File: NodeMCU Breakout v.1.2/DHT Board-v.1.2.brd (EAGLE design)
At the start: 42.8 x 54.6 mm, 13 parts, among them IC1 74HCT125N

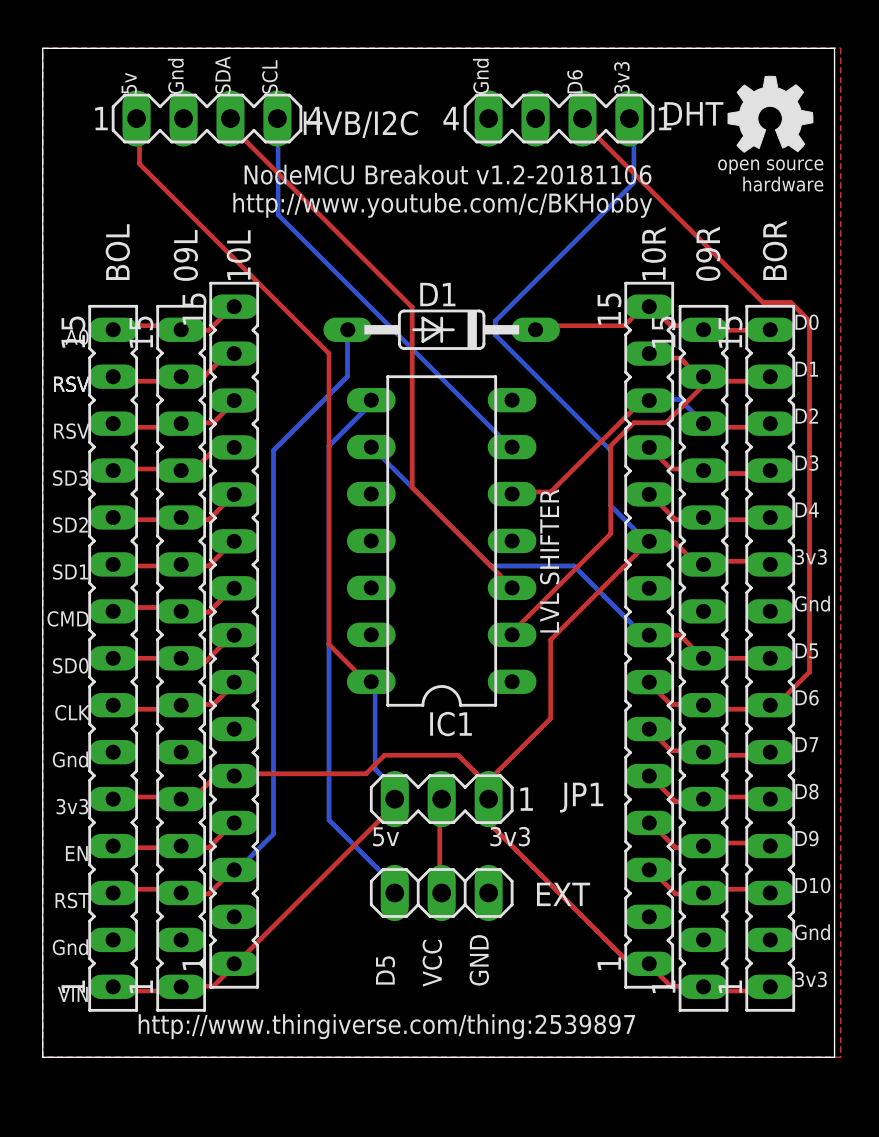
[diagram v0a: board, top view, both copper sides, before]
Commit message: 12/26/18(BK): Updated with changes to EXT signal (D4, to make it compatible with all LED drivers), adding another pin to the I2C/HVB header, and adding a set of solder jumpers on the back of the board, for bypassing the level shifter as necessary.
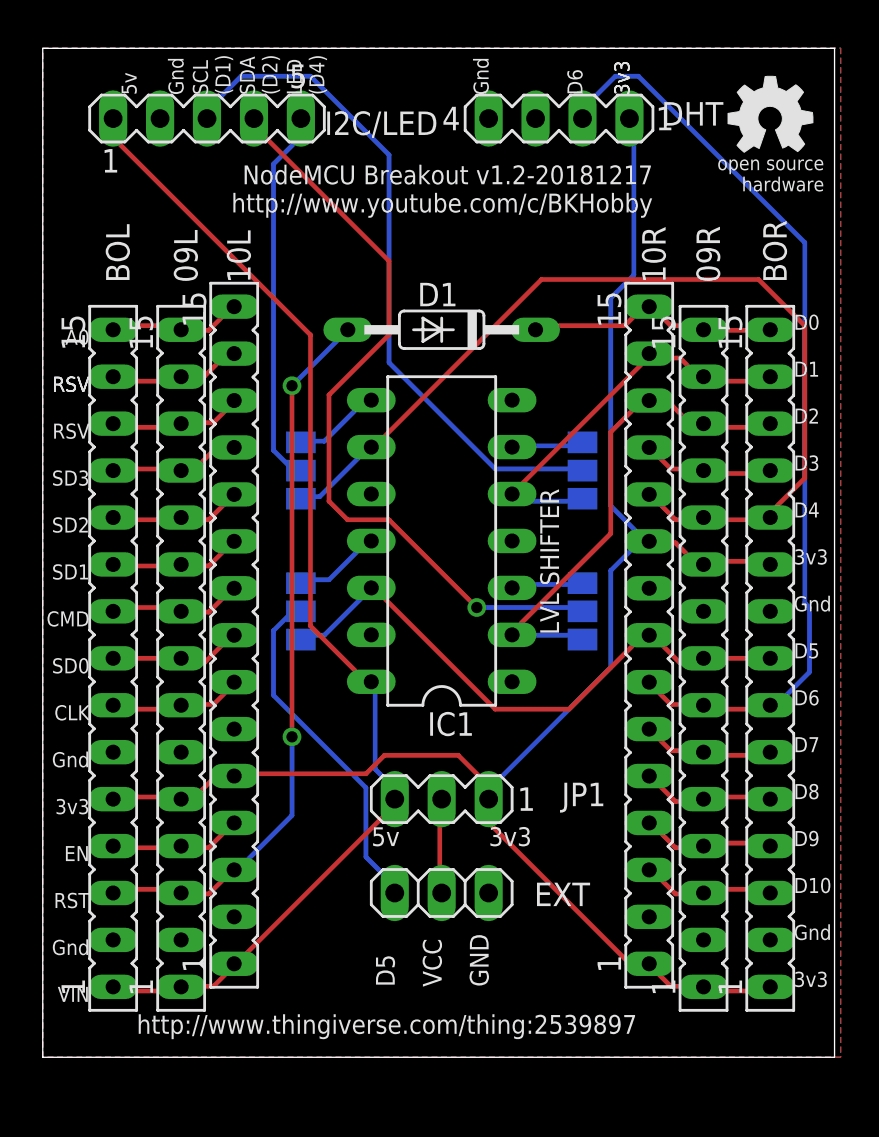
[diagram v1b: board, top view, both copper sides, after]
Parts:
- removed HVB/I2C: (no value), con-lstb:MA04-1
- added D1BYP, D2BYP, D4BYP, D5BYP: (no value), jumper:SJ_2
- added I2C/LED: (no value), con-lstb:MA05-1
- added U$2: (no value), oshw:OSHW_5MM
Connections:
- removed net SCL/D2: HVB/I2C.4, IC1.6
- removed net SDA/D1: HVB/I2C.3, IC1.3
- new net EXTD5: D5BYP.2, EXT.1
- new net HD1: D1BYP.3, IC1.6
- new net HD2: D2BYP.3, IC1.3
- new net HD4: D4BYP.3, IC1.8
- new net LED/D4: D4BYP.2, I2C/LED.5
- new net SCL/D1: D1BYP.2, I2C/LED.3
- new net SDA/D2: D2BYP.2, I2C/LED.4
- net 5V: now also I2C/LED.1; no longer HVB/I2C.1
- net D1: now also D1BYP.1, IC1.5; no longer IC1.2
- net D2: now also D2BYP.1, IC1.2; no longer IC1.5
- net D4: now also D4BYP.1, IC1.9
- net D5: now also D5BYP.1, IC1.12; no longer IC1.9
- net GND: now also I2C/LED.2, IC1.13; no longer HVB/I2C.2
- net HD5: now also D5BYP.3, IC1.11; no longer EXT.1, IC1.8
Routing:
- net D4: track 7.28 -> 51.9 mm
- net SDA/D2: track 0.00 -> 41.4 mm, vias 0 -> 1
- net SCL/D1: track 0.00 -> 37.0 mm
- net SDA/D1: track 31.8 -> 0.00 mm
- net HD5: track 29.2 -> 5.02 mm
- net SCL/D2: track 23.1 -> 0.00 mm
- net LED/D4: track 0.00 -> 20.5 mm
- net EXTD5: track 0.00 -> 19.0 mm
- net D2: track 16.9 -> 27.2 mm
- net D5: track 26.3 -> 31.8 mm
- net HD4: track 0.00 -> 4.87 mm
- net 3.3V: track 97.8 -> 93.0 mm
- net D1: track 26.8 -> 22.3 mm
- net D6: track 46.3 -> 50.7 mm
- net HD2: track 0.00 -> 3.94 mm
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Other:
- board text added: "BYP"
- board text added: "LED (D4)"
- board text added: "NodeMCU Breakout v1.2-20181217 http://www.youtube.com/c/BKHobby"
- board text added: "SCL (D1)"
- board text added: "SDA (D2)"
- board text added: "SHFT"
- board text removed: "NodeMCU Breakout v1.2-20181106 http://www.youtube.com/c/BKHobby"
- board text removed: "SCL"
- board text removed: "SDA"

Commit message: Updated to add I2C_VCC selector solder bridge (3.3/5v supply) and mounting holes.
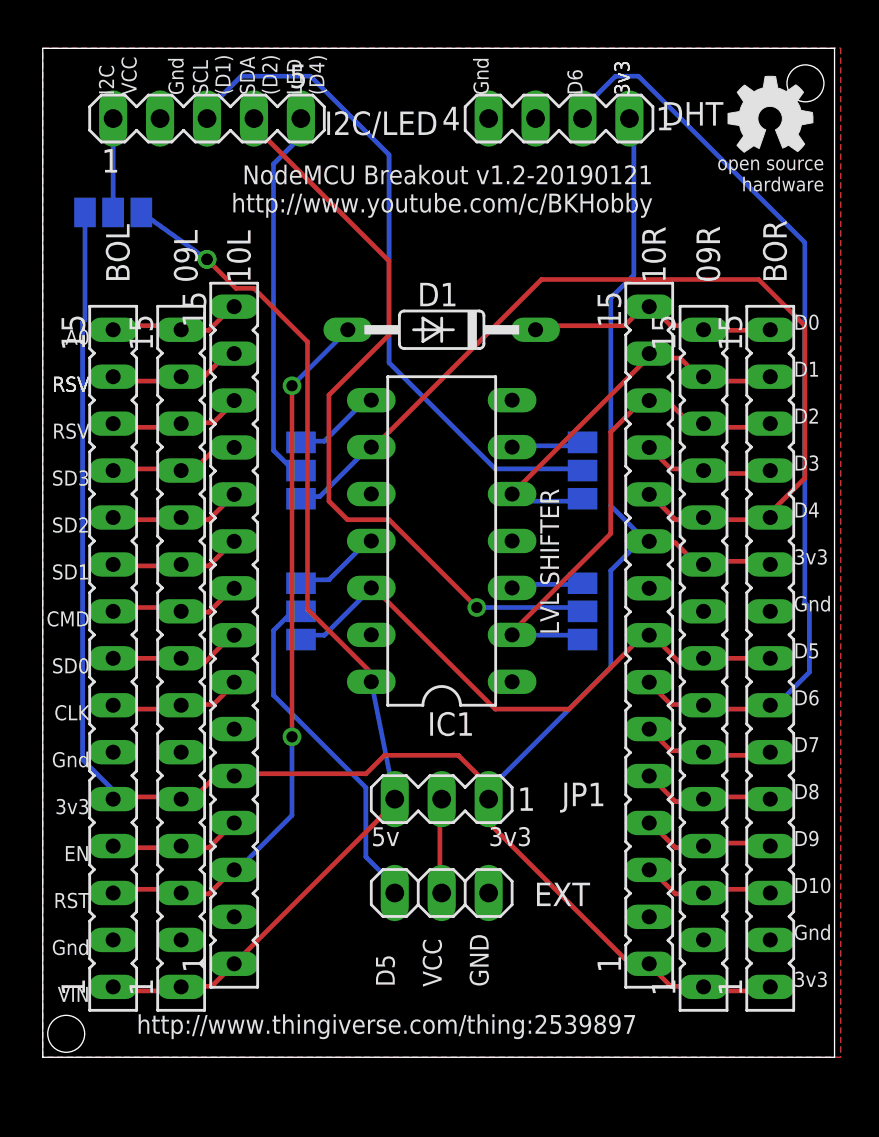
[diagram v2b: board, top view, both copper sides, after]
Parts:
- added I2C_VCC: (no value), jumper:SJ_2
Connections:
- new net I2C_VCC: I2C/LED.1, I2C_VCC.2
- net 3.3V: now also I2C_VCC.1
- net 5V: now also I2C_VCC.3; no longer I2C/LED.1
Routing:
- net 3.3V: track 93.0 -> 125.5 mm
- net 5V: track 63.8 -> 58.7 mm, vias 0 -> 1
- net I2C_VCC: track 0.00 -> 5.08 mm
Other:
- board text added: "3.3V"
- board text added: "5V"
- board text added: "I2C VCC"
- board text added: "NodeMCU Breakout v1.2-20190121 http://www.youtube.com/c/BKHobby"
- board text removed: "NodeMCU Breakout v1.2-20181217 http://www.youtube.com/c/BKHobby"
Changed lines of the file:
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@@
 <layer number="43" name="vRestrict" color="2" fill="10" visible="yes" active="yes"/>
 <layer number="44" name="Drills" color="7" fill="1" visible="no" active="yes"/>
-<layer number="45" name="Holes" color="7" fill="1" visible="no" active="yes"/>
+<layer number="45" name="Holes" color="7" fill="1" visible="yes" active="yes"/>
 <layer number="46" name="Milling" color="3" fill="1" visible="no" active="yes"/>
 <layer number="47" name="Measures" color="7" fill="1" visible="yes" active="yes"/>
@@
 <wire x1="59.36" y1="64.76" x2="16.51" y2="64.76" width="0" layer="20"/>
 <wire x1="16.51" y1="64.76" x2="16.51" y2="10.16" width="0" layer="20"/>
-<text x="49.53" y="58.42" size="1.016" layer="25" rot="R180">NodeMCU Breakout v1.2-20181217
+<text x="49.53" y="58.42" size="1.016" layer="25" rot="R180">NodeMCU Breakout v1.2-20190121
 http://www.youtube.com/c/BKHobby</text>
 <text x="38.1" y="13.97" size="1.016" layer="25" rot="R90">VCC</text>
@@
 <text x="34.29" y="21.59" size="1.016" layer="25">5v</text>
 <text x="40.64" y="21.59" size="1.016" layer="25">3v3</text>
-<text x="21.59" y="62.23" size="0.8128" layer="25" rot="R90">5v</text>
+<text x="21.59" y="62.23" size="0.8128" layer="25" rot="R90">I2C
+VCC</text>
 <text x="40.64" y="62.23" size="0.8128" layer="25" rot="R90">Gnd</text>
 <text x="24.13" y="62.23" size="0.8128" layer="25" rot="R90">Gnd</text>
@@
 <text x="29.21" y="38.1" size="0.8128" layer="26" rot="MR180">SHFT</text>
 <text x="44.45" y="38.1" size="0.8128" layer="26" rot="MR180">SHFT</text>
-<text x="22.86" y="58.42" size="1.016" layer="26" rot="MR180">NodeMCU Breakout v1.2-20181217
+<text x="22.86" y="58.42" size="1.016" layer="26" rot="MR180">NodeMCU Breakout v1.2-20190121
 http://www.youtube.com/c/BKHobby</text>
 <text x="53.34" y="11.43" size="1.016" layer="26" rot="MR0">http://www.thingiverse.com/thing:2539897</text>
+<text x="21.59" y="54.61" size="0.8128" layer="26" rot="MR180">5V</text>
+<text x="19.05" y="54.61" size="0.8128" layer="26" rot="MR180">3.3V</text>
+<text x="17.78" y="54.61" size="0.8128" layer="26" rot="MR180">3.3V</text>
+<hole x="57.785" y="62.865" drill="2"/>
+<hole x="17.78" y="11.43" drill="2"/>
 </plain>
 <attributes>
@@
 <autorouter>
 <pass name="Default">
-<param name="RoutingGrid" value="0.125mm"/>
+<param name="RoutingGrid" value="0.25mm"/>
 <param name="AutoGrid" value="1"/>
 <param name="Efforts" value="2"/>
@@
 </element>
 <element name="U$2" library="oshw" package="OSHW_5MM" value="" x="55.88" y="60.96" smashed="yes" rot="MR0"/>
+<element name="I2C_VCC" library="jumper" library_urn="urn:adsk.eagle:library:252" package="SJ_2" package3d_urn="urn:adsk.eagle:package:15474/1" value="" x="20.32" y="55.88" smashed="yes" rot="MR180">
+<attribute name="NAME" x="24.257" y="57.15" size="1.27" layer="26" ratio="10" rot="MR358.9"/>
+<attribute name="VALUE" x="20.2199" y="55.88" size="0.02" layer="28" rot="MR180"/>
+</element>
 </elements>
 <signals>
@@
 <wire x1="24" y1="21.5" x2="24" y2="21.59" width="0.254" layer="1"/>
 </signal>
+<signal name="I2C_VCC">
+<contactref element="I2C/LED" pad="1"/>
+<contactref element="I2C_VCC" pad="2"/>
+<wire x1="20.32" y1="55.88" x2="20.32" y2="60.96" width="0.254" layer="16"/>
+</signal>
 <signal name="5V">
 <contactref element="10L" pad="1"/>
 <contactref element="09L" pad="1"/>
 <contactref element="JP1" pad="3"/>
-<contactref element="I2C/LED" pad="1"/>
 <contactref element="IC1" pad="14"/>
 <contactref element="BOL" pad="1"/>
@@
 <wire x1="20.5" y1="13.75" x2="20.32" y2="13.97" width="0.254" layer="1"/>
 <wire x1="24" y1="13.75" x2="24" y2="13.97" width="0.254" layer="1"/>
-<wire x1="25.75" y1="14" x2="26.75" y2="15" width="0.254" layer="1"/>
-<wire x1="24" y1="14" x2="25.75" y2="14" width="0.254" layer="1"/>
-<wire x1="26.75" y1="15" x2="26.87" y2="15.22" width="0.254" layer="1"/>
+<wire x1="24" y1="14" x2="25.65" y2="14" width="0.254" layer="1"/>
+<wire x1="25.65" y1="14" x2="25.75" y2="14" width="0.254" layer="1"/>
 <wire x1="24" y1="14" x2="24" y2="13.97" width="0.254" layer="1"/>
-<wire x1="34.5" y1="25.75" x2="34.5" y2="30.25" width="0.254" layer="16"/>
-<wire x1="35.5" y1="24.75" x2="34.5" y2="25.75" width="0.254" layer="16"/>
-<wire x1="35.5" y1="24.25" x2="35.5" y2="24.75" width="0.254" layer="16"/>
 <wire x1="34.5" y1="30.25" x2="34.29" y2="30.48" width="0.254" layer="16"/>
 <wire x1="35.5" y1="24.25" x2="35.56" y2="24.13" width="0.254" layer="16"/>
-<wire x1="20.5" y1="59.75" x2="20.5" y2="60.75" width="0.254" layer="1"/>
-<wire x1="31" y1="49.25" x2="20.5" y2="59.75" width="0.254" layer="1"/>
-<wire x1="31" y1="33.5" x2="31" y2="49.25" width="0.254" layer="1"/>
-<wire x1="34.25" y1="30.25" x2="31" y2="33.5" width="0.254" layer="1"/>
-<wire x1="20.5" y1="60.75" x2="20.32" y2="60.96" width="0.254" layer="1"/>
 <wire x1="34.25" y1="30.25" x2="34.29" y2="30.48" width="0.254" layer="1"/>
-<wire x1="35.75" y1="24" x2="27" y2="15.25" width="0.254" layer="1"/>
-<wire x1="27" y1="15.25" x2="26.87" y2="15.22" width="0.254" layer="1"/>
-<wire x1="35.75" y1="24" x2="35.56" y2="24.13" width="0.254" layer="1"/>
+<contactref element="I2C_VCC" pad="3"/>
+<wire x1="25.65" y1="14" x2="26.87" y2="15.22" width="0.254" layer="1"/>
+<wire x1="26.87" y1="15.22" x2="35.56" y2="23.91" width="0.254" layer="1"/>
+<wire x1="35.56" y1="23.91" x2="35.56" y2="24.13" width="0.254" layer="1"/>
+<wire x1="35.56" y1="24.13" x2="34.29" y2="30.48" width="0.254" layer="16"/>
+<wire x1="34.29" y1="30.48" x2="34.29" y2="30.958675" width="0.254" layer="1"/>
+<wire x1="27.940725" y1="51.7706" x2="26.9694" y2="51.7706" width="0.254" layer="1"/>
+<wire x1="34.29" y1="30.958675" x2="30.8382" y2="34.410475" width="0.254" layer="1"/>
+<wire x1="30.8382" y1="34.410475" x2="30.8382" y2="48.873125" width="0.254" layer="1"/>
+<wire x1="30.8382" y1="48.873125" x2="27.940725" y2="51.7706" width="0.254" layer="1"/>
+<wire x1="26.9694" y1="51.7706" x2="25.4" y2="53.34" width="0.254" layer="1"/>
+<via x="25.4" y="53.34" extent="1-16" drill="0.6096"/>
+<wire x1="25.4" y1="53.34" x2="21.844" y2="55.88" width="0.254" layer="16"/>
 </signal>
 <signal name="N$1">
@@
 <wire x1="49" y1="38.25" x2="49.33" y2="38.08" width="0.254" layer="16"/>
 <wire x1="40.75" y1="24.25" x2="40.64" y2="24.13" width="0.254" layer="16"/>
+<contactref element="I2C_VCC" pad="1"/>
+<wire x1="20.32" y1="24.13" x2="20.32" y2="24.608675" width="0.254" layer="16"/>
+<wire x1="18.669" y1="49.940325" x2="18.796" y2="50.067325" width="0.254" layer="16"/>
+<wire x1="18.796" y1="50.067325" x2="18.796" y2="55.88" width="0.254" layer="16"/>
+<wire x1="20.32" y1="24.608675" x2="18.669" y2="26.259675" width="0.254" layer="16"/>
+<wire x1="18.669" y1="26.259675" x2="18.669" y2="49.940325" width="0.254" layer="16"/>
 </signal>
 <signal name="D1">
@@
 <contactref element="IC1" pad="4"/>
 <contactref element="IC1" pad="1"/>
-<wire x1="41.91" y1="45.72" x2="40.64" y2="60.96" width="0" layer="19" extent="1-1"/>
-<wire x1="41.91" y1="38.1" x2="41.91" y2="45.72" width="0" layer="19" extent="1-1"/>
-<wire x1="41.91" y1="30.48" x2="41.91" y2="38.1" width="0" layer="19" extent="1-1"/>
-<wire x1="49.33" y1="35.54" x2="41.91" y2="38.1" width="0" layer="19" extent="1-1"/>
-<wire x1="52.27" y1="34.29" x2="49.33" y2="35.54" width="0" layer="19" extent="1-1"/>
-<wire x1="55.88" y1="34.29" x2="52.27" y2="34.29" width="0" layer="19" extent="1-1"/>
-<wire x1="34.29" y1="40.64" x2="41.91" y2="38.1" width="0" layer="19" extent="1-1"/>
-<wire x1="34.29" y1="33.02" x2="34.29" y2="40.64" width="0" layer="19" extent="1-1"/>
-<wire x1="26.87" y1="27.92" x2="34.29" y2="33.02" width="0" layer="19" extent="1-1"/>
-<wire x1="24" y1="26.67" x2="26.87" y2="27.92" width="0" layer="19" extent="1-1"/>
-<wire x1="20.32" y1="26.67" x2="24" y2="26.67" width="0" layer="19" extent="1-1"/>
-<wire x1="26.87" y1="17.76" x2="24" y2="26.67" width="0" layer="19" extent="1-1"/>
-<wire x1="24" y1="16.51" x2="26.87" y2="17.76" width="0" layer="19" extent="1-1"/>
-<wire x1="20.32" y1="16.51" x2="24" y2="16.51" width="0" layer="19" extent="1-1"/>
-<wire x1="40.64" y1="19.05" x2="41.91" y2="30.48" width="0" layer="19" extent="1-1"/>
-<wire x1="49.33" y1="17.76" x2="40.64" y2="19.05" width="0" layer="19" extent="1-1"/>
-<wire x1="52.27" y1="16.51" x2="49.33" y2="17.76" width="0" layer="19" extent="1-1"/>
-<wire x1="55.88" y1="16.51" x2="52.27" y2="16.51" width="0" layer="19" extent="1-1"/>
-<wire x1="22.86" y1="60.96" x2="40.64" y2="60.96" width="0" layer="19" extent="1-1"/>
 </signal>
 <signal name="CLK">
@@
 <wire x1="34.25" y1="38.25" x2="34.29" y2="38.1" width="0.254" layer="16"/>
 </signal>
+<signal name="N$2">
+<via x="25.4" y="53.34" extent="1-16" drill="0.6096"/>
+</signal>
 </signals>

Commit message: 2/2/19(BK): Updated rev 1.2 to final:
-Removed I2C_VCC Solder jumper and added 6th pin to the header (both 3.3v & 5v are brought out)
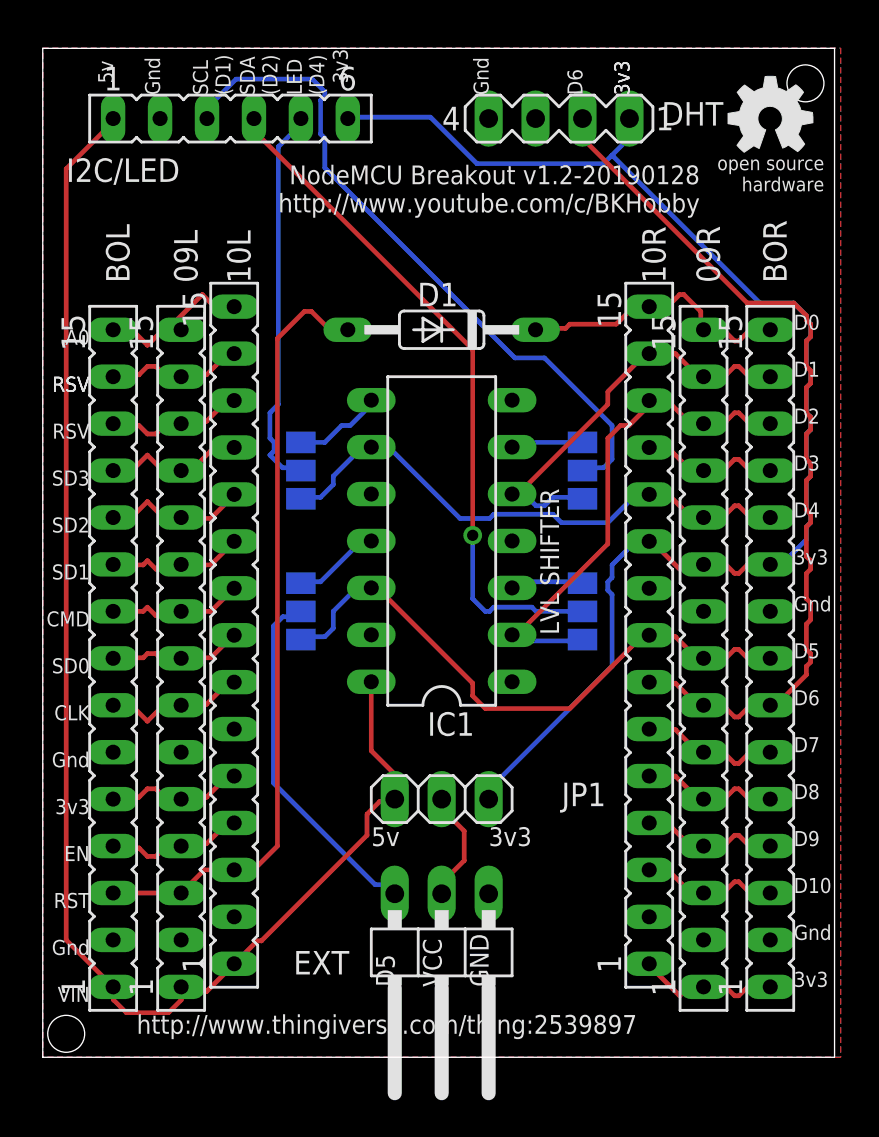
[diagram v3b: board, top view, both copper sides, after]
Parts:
- removed I2C_VCC: (no value), jumper:SJ_2
- EXT: device pinhead:1X03 -> pinhead:1X03/90
- I2C/LED: device con-lstb:MA05-1 -> con-lsta:FE06
- JP1: device con-lstb:MA03-1 -> pinhead:1X03
- moved EXT 3.85 mm to (38.1, 15.2), turned to 180 degrees
- moved I2C/LED 1.27 mm to (26.7, 61.0)
- moved U$2 1.27 mm to (54.6, 61.0)
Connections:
- removed net I2C_VCC: I2C/LED.1, I2C_VCC.2
- new net 3.3V(1): 09R.1, 10R.1, BOR.1
- new net 3.3V(3): 09L.5, 10L.5, BOL.5
- net 3.3V: now also I2C/LED.6; no longer 09L.5, 09R.1, 10L.5, 10R.1, BOL.5, BOR.1, I2C_VCC.1
- net 5V: now also I2C/LED.1; no longer I2C_VCC.3
- net EXTD5: now also EXT.3; no longer EXT.1
- net GND: now also EXT.1; no longer EXT.3
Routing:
- net 3.3V: track 125.5 -> 73.5 mm
- net 5V: track 58.7 -> 80.5 mm, vias 1 -> 0
- net D4: track 51.9 -> 30.5 mm
- net 3.3V(1): track 0.00 -> 7.88 mm
- net 3.3V(3): track 0.00 -> 7.60 mm
- net I2C_VCC: track 5.08 -> 0.00 mm
- net SDA/D2: track 41.4 -> 37.3 mm
- net RST: track 39.3 -> 42.2 mm, vias 2 -> 0
- net D6: track 50.7 -> 48.7 mm
- net A0: track 7.43 -> 9.08 mm
- net D5: track 31.8 -> 33.2 mm
- net D0: track 14.2 -> 15.4 mm
- net VSS: track 5.14 -> 6.10 mm
- net LED/D4: track 20.5 -> 21.3 mm
- net SD3: track 7.16 -> 7.92 mm
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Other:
- board text added: "NodeMCU Breakout v1.2-20190128 http://www.youtube.com/c/BKHobby"
- board text removed: "3.3V"
- board text removed: "5V"
- board text removed: "I2C VCC"
- board text removed: "NodeMCU Breakout v1.2-20190121 http://www.youtube.com/c/BKHobby"
